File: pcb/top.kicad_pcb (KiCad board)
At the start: 2 copper layers, 186 x 28 mm, 65 parts, among them J1 Conn_01x01, J10 Conn_01x01, J11 Conn_01x01, J2 Conn_01x01, J3 Conn_01x06, J4 Conn_01x01, J5 Conn_01x01, J6 Conn_01x01, J7 Conn_01x01, J8 Conn_01x01, J9 Conn_01x01, Q1 2N7002, Q2 2N7002, Q3 2N7002, Q4 2N7002, U1 L78L05_SOT89, U2 PIC12F629-ISN

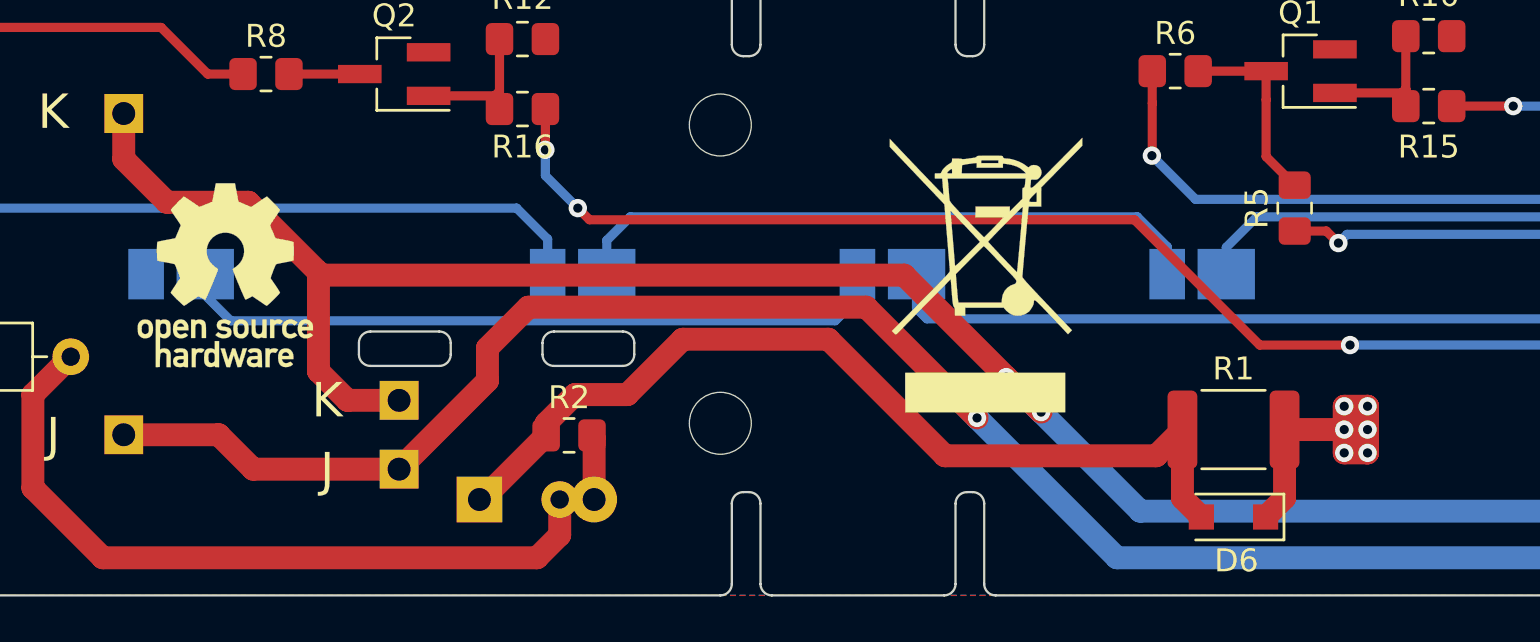
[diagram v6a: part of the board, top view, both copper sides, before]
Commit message: Use 2512 power resistor.
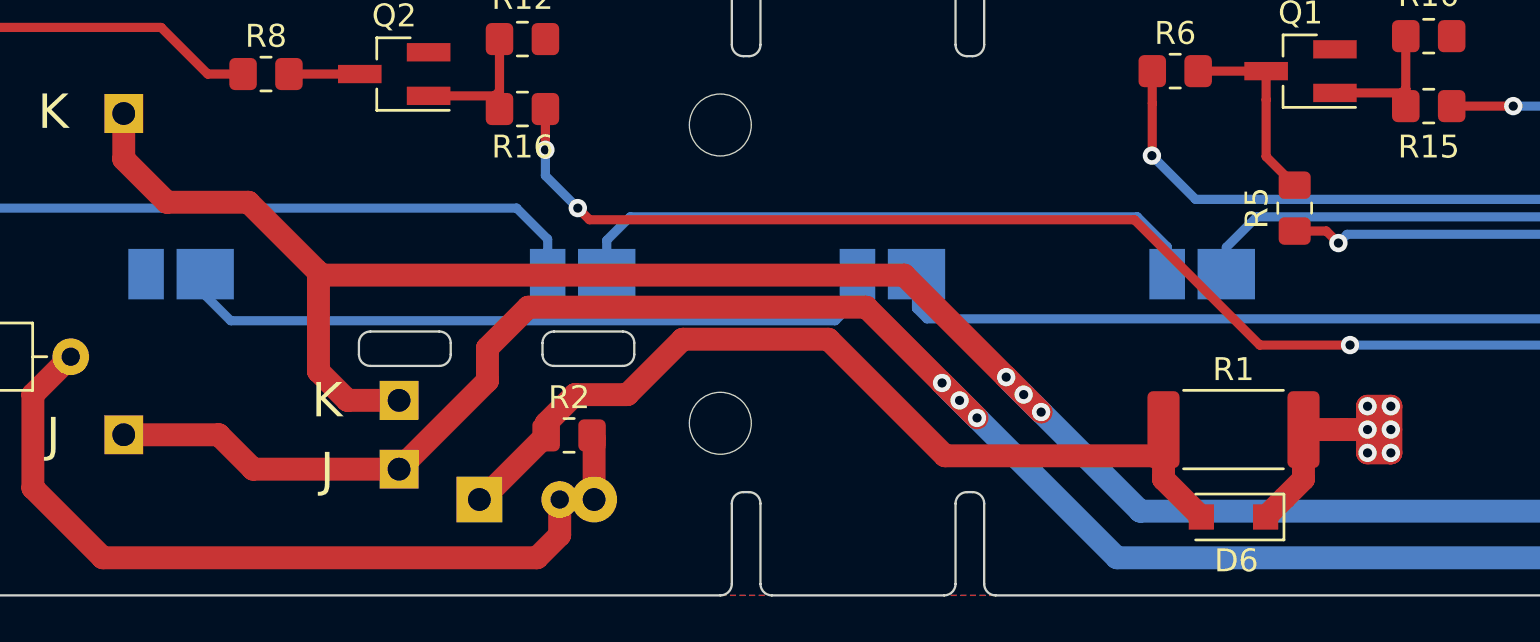
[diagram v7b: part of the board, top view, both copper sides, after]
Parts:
- removed REF**: OSHW-Logo_7.5x8mm_SilkScreen, Symbol:OSHW-Logo_7.5x8mm_SilkScreen
- removed REF**: WEEE-Logo_8.4x12mm_SilkScreen, Symbol:WEEE-Logo_8.4x12mm_SilkScreen
- C2: value 47u -> 47u/6.3V
- R1: footprint Resistor_SMD:R_1812_4532Metric_Pad1.30x3.40mm_HandSolder -> Resistor_SMD:R_2512_6332Metric_Pad1.40x3.35mm_HandSolder
- R10, R12, R13, R14, R7: value 10k -> 100k
- R15, R16, R17, R18: value 250R -> 220R
- R3, R4, R5, R6, R8, R9: value R -> 10k
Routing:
- net Net-(C3-Pad1): track 40.6 -> 39.3 mm
- net +15V: track 34.2 -> 34.7 mm

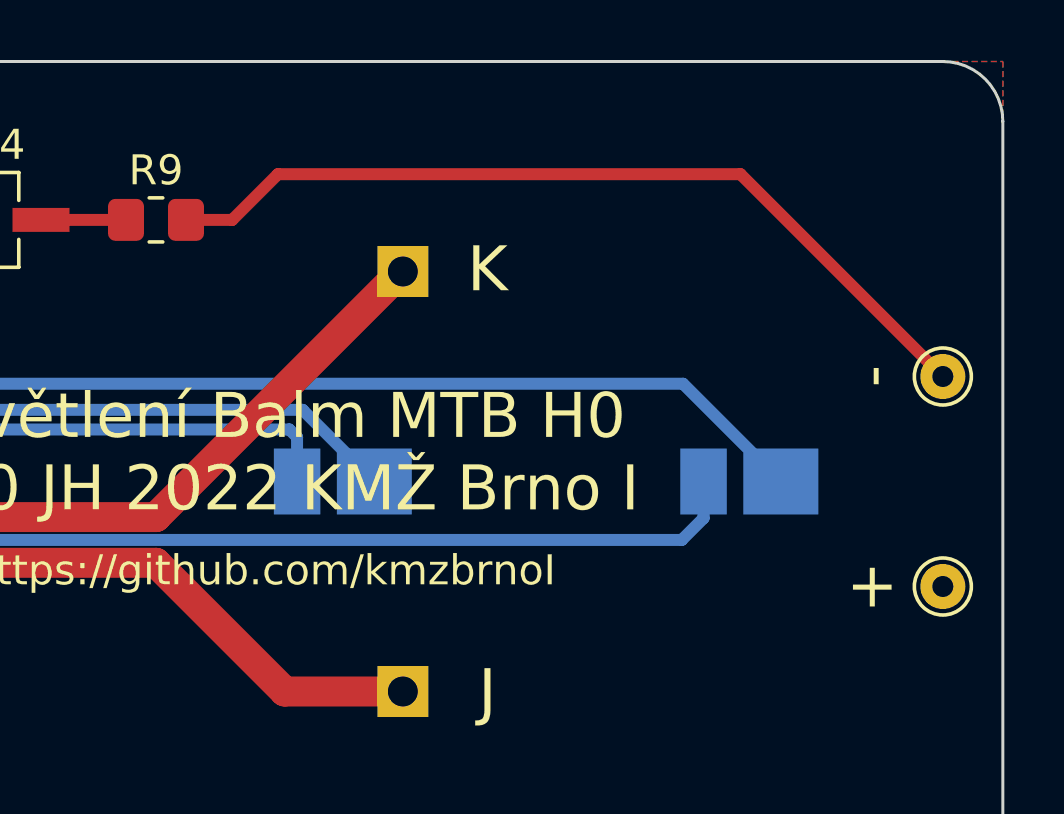
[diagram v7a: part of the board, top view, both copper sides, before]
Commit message: Top: switch +-.
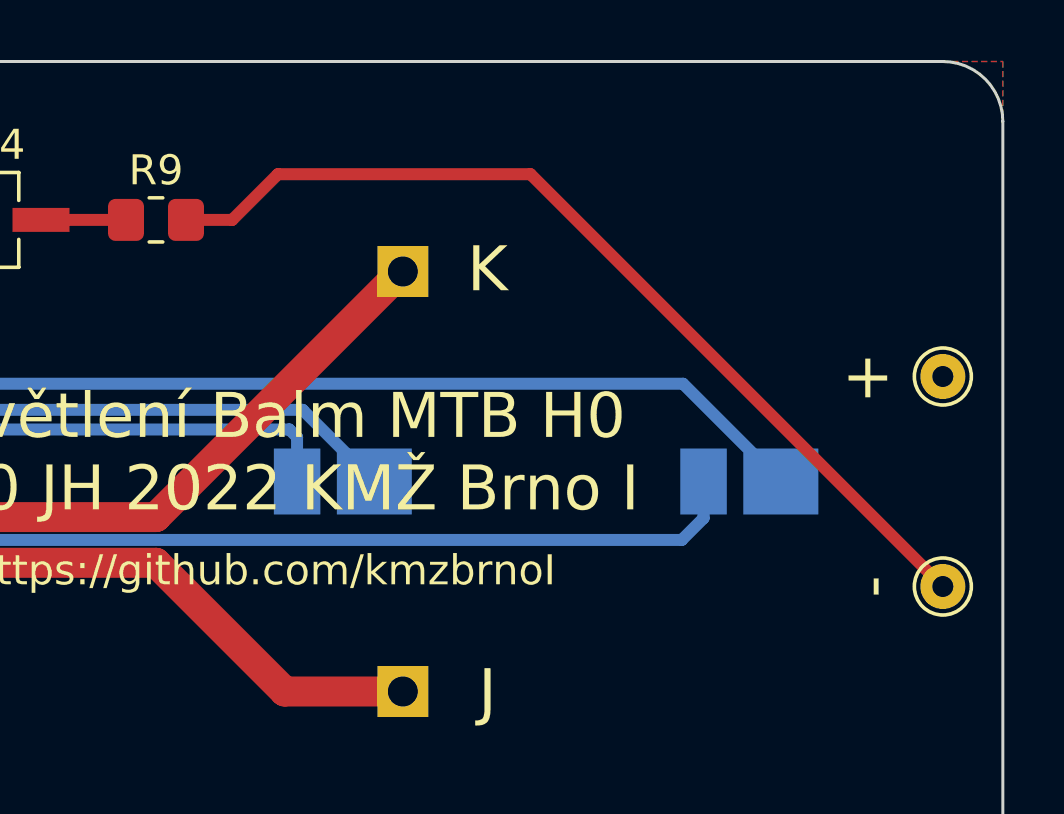
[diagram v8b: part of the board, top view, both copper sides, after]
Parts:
- moved J7 7.00 mm to (234.0, 86.5)
- moved J9 7.00 mm to (234.0, 93.5)
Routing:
- net Net-(J9-Pad1): track 28.7 -> 31.6 mm
